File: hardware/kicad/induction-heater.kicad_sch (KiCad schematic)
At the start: 20 parts, among them Q1 Q_NMOS_DGS, Q2 Q_NMOS_DGS

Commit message: next
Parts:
- D1: Spice_Model D -> (none); Spice_Netlist_Enabled Y -> (none); Spice_Primitive D -> (none)
- D5: Spice_Model (none) -> D_Zener; Spice_Netlist_Enabled (none) -> Y; Spice_Primitive (none) -> D
- Q1, Q2: Spice_Model (none) -> Q_NMOS_DGS; Spice_Netlist_Enabled (none) -> Y; Spice_Primitive (none) -> M
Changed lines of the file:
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@@
     (effects (font (size 1.27 1.27)) (justify left bottom))
+  )
+  (symbol (lib_id "Device:D_Zener") (at 22.86 27.94 270) (unit 1)
+    (in_bom yes) (on_board yes) (fields_autoplaced)
+    (property "Reference" "D1" (id 0) (at 25.4 26.6699 90)
+      (effects (font (size 1.27 1.27)) (justify left))
+    )
+    (property "Value" "D_Zener" (id 1) (at 25.4 29.2099 90)
+      (effects (font (size 1.27 1.27)) (justify left))
+    )
+    (property "Footprint" "" (id 2) (at 22.86 27.94 0)
+      (effects (font (size 1.27 1.27)) hide)
+    )
+    (property "Datasheet" "~" (id 3) (at 22.86 27.94 0)
+      (effects (font (size 1.27 1.27)) hide)
+    )
+    (pin "1")
+    (pin "2")
   )
   (symbol (lib_id "power:GND") (at 111.76 88.9 0) (unit 1)
@@
       (effects (font (size 1.27 1.27)) hide)
     )
+    (property "Spice_Primitive" "M" (id 4) (at 134.62 76.2 0)
+      (effects (font (size 1.27 1.27)) hide)
+    )
+    (property "Spice_Model" "Q_NMOS_DGS" (id 5) (at 134.62 76.2 0)
+      (effects (font (size 1.27 1.27)) hide)
+    )
+    (property "Spice_Netlist_Enabled" "Y" (id 6) (at 134.62 76.2 0)
+      (effects (font (size 1.27 1.27)) hide)
+    )
     (pin "1")
     (pin "2")
@@
     )
     (property "Spice_Netlist_Enabled" "Y" (id 6) (at 111.76 68.58 0)
-      (effects (font (size 1.27 1.27)) hide)
-    )
-    (pin "1")
-    (pin "2")
-  )
-  (symbol (lib_id "Device:D_Zener") (at 22.86 27.94 270) (unit 1)
-    (in_bom yes) (on_board yes) (fields_autoplaced)
-    (property "Reference" "D1" (id 0) (at 25.4 26.6699 90)
-      (effects (font (size 1.27 1.27)) (justify left))
-    )
-    (property "Value" "D_Zener" (id 1) (at 25.4 29.2099 90)
-      (effects (font (size 1.27 1.27)) (justify left))
-    )
-    (property "Footprint" "" (id 2) (at 22.86 27.94 0)
-      (effects (font (size 1.27 1.27)) hide)
-    )
-    (property "Datasheet" "~" (id 3) (at 22.86 27.94 0)
-      (effects (font (size 1.27 1.27)) hide)
-    )
-    (property "Spice_Primitive" "D" (id 4) (at 22.86 27.94 0)
-      (effects (font (size 1.27 1.27)) hide)
-    )
-    (property "Spice_Model" "D" (id 5) (at 22.86 27.94 0)
-      (effects (font (size 1.27 1.27)) hide)
-    )
-    (property "Spice_Netlist_Enabled" "Y" (id 6) (at 22.86 27.94 0)
       (effects (font (size 1.27 1.27)) hide)
     )
@@
       (effects (font (size 1.27 1.27)) hide)
     )
+    (property "Spice_Primitive" "D" (id 4) (at 111.76 82.55 0)
+      (effects (font (size 1.27 1.27)) hide)
+    )
+    (property "Spice_Model" "D_Zener" (id 5) (at 111.76 82.55 0)
+      (effects (font (size 1.27 1.27)) hide)
+    )
+    (property "Spice_Netlist_Enabled" "Y" (id 6) (at 111.76 82.55 0)
+      (effects (font (size 1.27 1.27)) hide)
+    )
     (pin "1")
     (pin "2")
@@
     )
     (property "Datasheet" "~" (id 3) (at 134.62 38.1 0)
+      (effects (font (size 1.27 1.27)) hide)
+    )
+    (property "Spice_Primitive" "M" (id 4) (at 134.62 38.1 0)
+      (effects (font (size 1.27 1.27)) hide)
+    )
+    (property "Spice_Model" "Q_NMOS_DGS" (id 5) (at 134.62 38.1 0)
+      (effects (font (size 1.27 1.27)) hide)
+    )
+    (property "Spice_Netlist_Enabled" "Y" (id 6) (at 134.62 38.1 0)
       (effects (font (size 1.27 1.27)) hide)
     )
@@
       (reference "C3") (unit 1) (value "4.7u") (footprint "")
     )
-    (path "/2d14997f-3535-4ad5-9243-33af41ad51f4"
+    (path "/00a8d501-612a-44b1-8671-7a3ee3d8d8a2"
       (reference "D1") (unit 1) (value "D_Zener") (footprint "")
     )

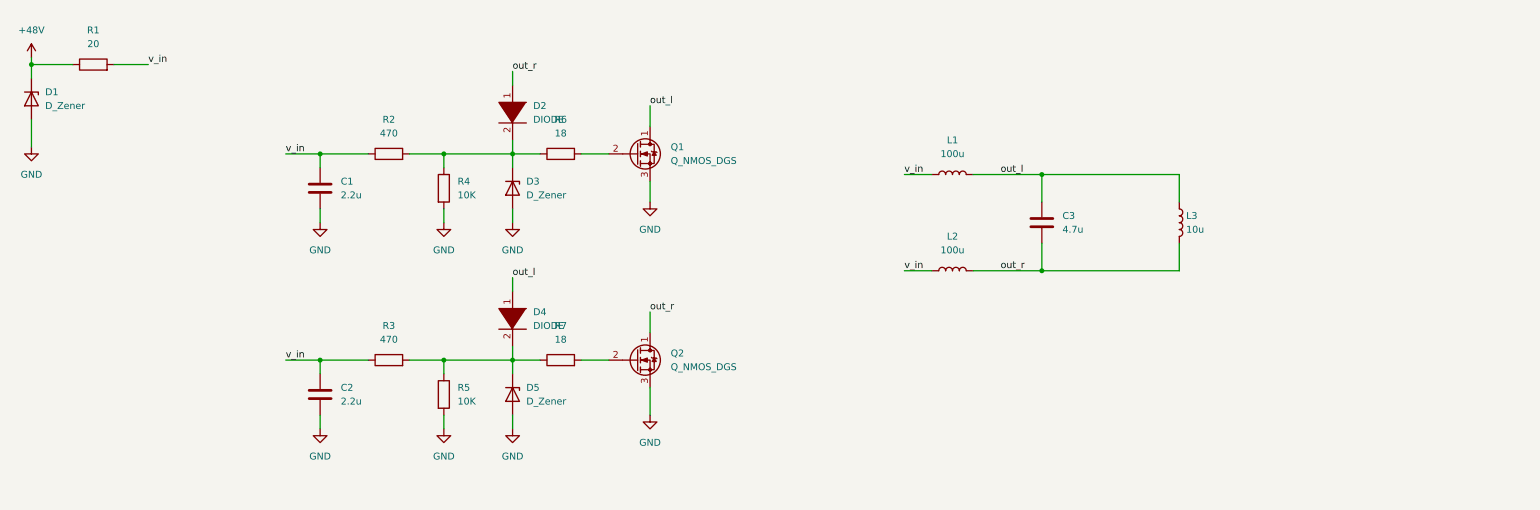
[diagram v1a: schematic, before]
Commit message: Components chosen and board layout made
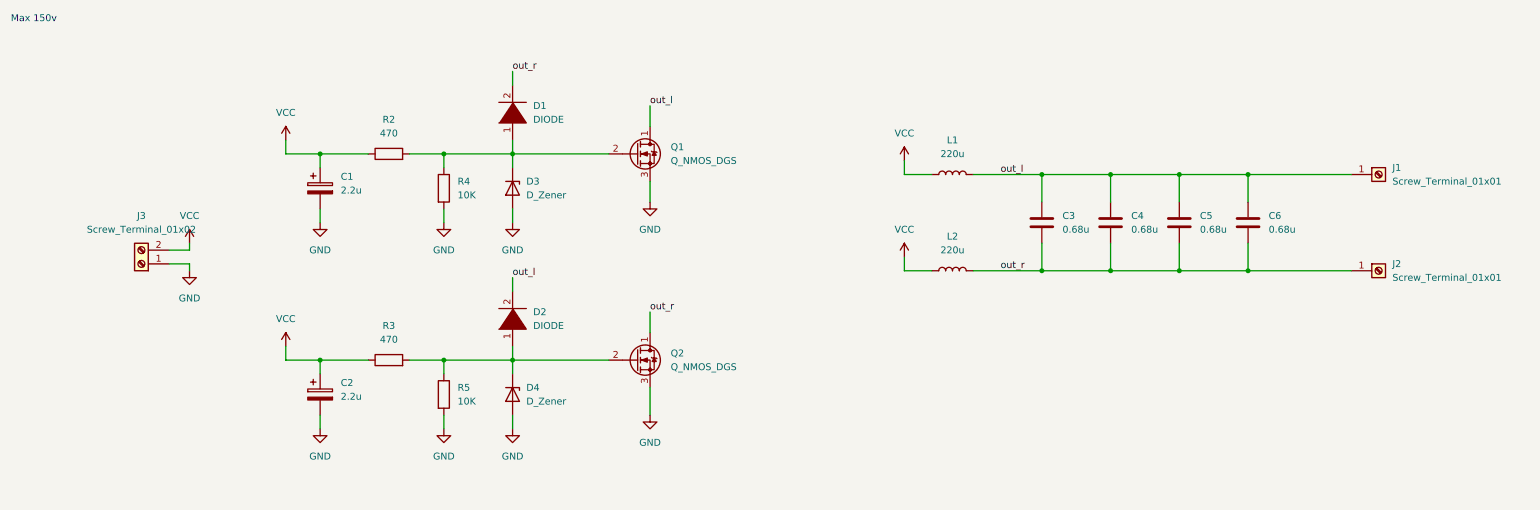
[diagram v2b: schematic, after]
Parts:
- removed C1, C2: 2.2u, symbol Device:C
- removed D1, D5: D_Zener, symbol Device:D_Zener
- removed D4: DIODE, symbol pspice:DIODE
- removed L3: 10u, symbol Device:L
- removed R1: 20, symbol Device:R
- removed R6, R7: 18, symbol Device:R
- added C1, C2: 2.2u, Capacitor_THT:CP_Radial_D6.3mm_P2.50mm, symbol Device:C_Polarized
- added C4, C5, C6: 0.68u, Capacitor_THT:C_Rect_L31.5mm_W15.0mm_P27.50mm_MKS4, symbol Device:C
- added D1: DIODE, Diode_THT:D_DO-41_SOD81_P7.62mm_Horizontal, symbol pspice:DIODE
- added D4: D_Zener, Diode_THT:D_DO-15_P12.70mm_Horizontal, symbol Device:D_Zener
- added J1, J2: Screw_Terminal_01x01, Connector:Banana_Jack_1Pin, symbol Connector:Screw_Terminal_01x01
- added J3: Screw_Terminal_01x02, Connector_Phoenix_MSTB:PhoenixContact_MSTBVA_2,5_2-G_1x02_P5.00mm_Vertical, symbol Connector:Screw_Terminal_01x02
- C3: value 4.7u -> 0.68u; footprint (none) -> Capacitor_THT:C_Rect_L31.5mm_W15.0mm_P27.50mm_MKS4; Max V (none) -> 1000; Mfr (none) -> MKS4O136806F00KYSD
- D2: footprint (none) -> Diode_THT:D_DO-41_SOD81_P7.62mm_Horizontal; Max V (none) -> 600; Mfr (none) -> UF4005-E3/54; Spice_Model DIODE -> (none); Spice_Netlist_Enabled Y -> (none); Spice_Primitive D -> (none)
- D3: footprint (none) -> Diode_THT:D_DO-15_P12.70mm_Horizontal; Mfr (none) -> 1N5349BG
- L1, L2: value 100u -> 220u; footprint (none) -> Inductor_THT:L_Toroid_Vertical_L31.8mm_W15.9mm_P13.50mm_Bourns_5700; Mfr (none) -> 2300HT-221-V-RC
- Q1, Q2: footprint (none) -> Package_TO_SOT_THT:TO-220-3_Vertical; Max V (none) -> 650; Mfr (none) -> NTP067N65S3H; Spice_Model Q_NMOS_DGS -> (none); Spice_Netlist_Enabled Y -> (none); Spice_Primitive M -> (none)
- R2, R3: footprint (none) -> Resistor_THT:R_Box_L8.4mm_W2.5mm_P5.08mm; Max V (none) -> 420; Mfr (none) -> AP851470RJ
- R4, R5: footprint (none) -> Resistor_THT:R_Axial_DIN0617_L17.0mm_D6.0mm_P20.32mm_Horizontal; Max V (none) -> 350; Mfr (none) -> ROX3SJ10K
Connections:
- net GND: now also C1.2, C2.2, D4.2 (A), J3.1 (Pin_1)
- net out_l: now also D2.2 (A), C4.1, C5.1, C6.1, J1.1 (Pin_1)
- net out_r: now also C4.2, C5.2, C6.2, D1.2 (A), J2.1 (Pin_1); no longer D2.1 (K)
- net at Q2.2 (G): now also D2.1 (K), R3.2, R5.1, D4.1 (K)
- net at D3.1 (K), R2.2, R4.1: now also Q1.2 (G), D1.1 (K); no longer D2.2 (A)
- net v_in renamed VCC
- net VCC: now also C1.1, C2.1, J3.2 (Pin_2)
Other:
- note added: "Max 150v"

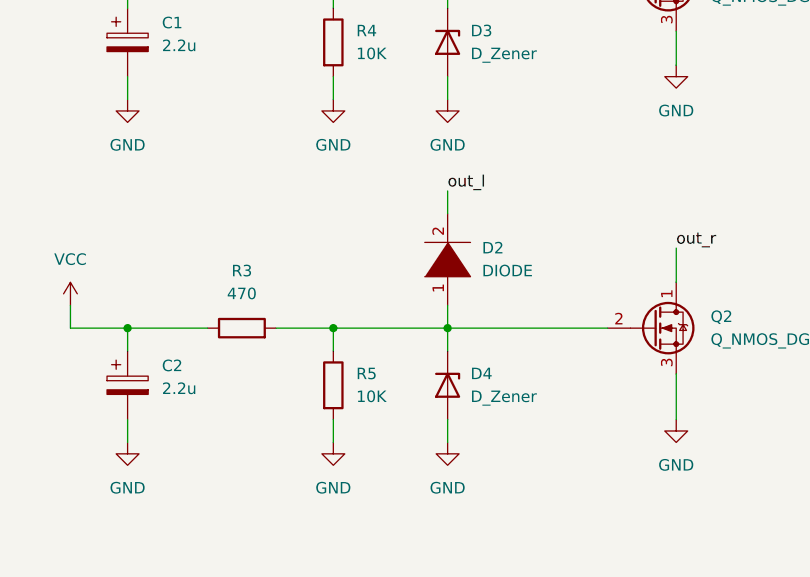
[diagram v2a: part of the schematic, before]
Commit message: Compacter board
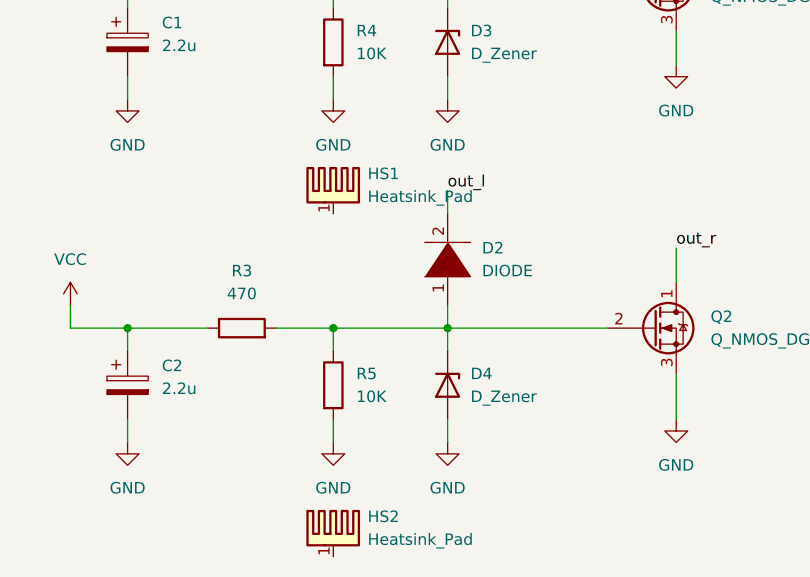
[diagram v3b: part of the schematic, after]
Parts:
- added HS1, HS2: Heatsink_Pad, Heatsink:Heatsink_Fischer_SK129-STS_42x25mm_2xDrill2.5mm, symbol Mechanical:Heatsink_Pad
- R4, R5: footprint Resistor_THT:R_Axial_DIN0617_L17.0mm_D6.0mm_P20.32mm_Horizontal -> Resistor_THT:R_Axial_DIN0207_L6.3mm_D2.5mm_P10.16mm_Horizontal
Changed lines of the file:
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@@
       (effects (font (size 1.27 1.27)) (justify left))
     )
-    (property "Footprint" "Resistor_THT:R_Axial_DIN0617_L17.0mm_D6.0mm_P20.32mm_Horizontal" (id 2) (at 97.282 82.55 90)
+    (property "Footprint" "Resistor_THT:R_Axial_DIN0207_L6.3mm_D2.5mm_P10.16mm_Horizontal" (id 2) (at 97.282 82.55 90)
       (effects (font (size 1.27 1.27)) hide)
     )
@@
     (pin "1")
     (pin "2")
+  )
+  (symbol (lib_id "Mechanical:Heatsink_Pad") (at 99.06 60.96 0) (unit 1)
+    (in_bom yes) (on_board yes) (fields_autoplaced)
+    (property "Reference" "HS1" (id 0) (at 102.87 59.0549 0)
+      (effects (font (size 1.27 1.27)) (justify left))
+    )
+    (property "Value" "Heatsink_Pad" (id 1) (at 102.87 61.5949 0)
+      (effects (font (size 1.27 1.27)) (justify left))
+    )
+    (property "Footprint" "Heatsink:Heatsink_Fischer_SK129-STS_42x25mm_2xDrill2.5mm" (id 2) (at 99.3648 62.23 0)
+      (effects (font (size 1.27 1.27)) hide)
+    )
+    (property "Datasheet" "~" (id 3) (at 99.3648 62.23 0)
+      (effects (font (size 1.27 1.27)) hide)
+    )
+    (property "Mfr" "6398BG" (id 4) (at 99.06 60.96 0)
+      (effects (font (size 1.27 1.27)) hide)
+    )
+    (pin "1")
   )
   (symbol (lib_id "power:VCC") (at 69.85 73.66 0) (unit 1)
@@
     (pin "1")
   )
+  (symbol (lib_id "Mechanical:Heatsink_Pad") (at 99.06 99.06 0) (unit 1)
+    (in_bom yes) (on_board yes) (fields_autoplaced)
+    (property "Reference" "HS2" (id 0) (at 102.87 97.1549 0)
+      (effects (font (size 1.27 1.27)) (justify left))
+    )
+    (property "Value" "Heatsink_Pad" (id 1) (at 102.87 99.6949 0)
+      (effects (font (size 1.27 1.27)) (justify left))
+    )
+    (property "Footprint" "Heatsink:Heatsink_Fischer_SK129-STS_42x25mm_2xDrill2.5mm" (id 2) (at 99.3648 100.33 0)
+      (effects (font (size 1.27 1.27)) hide)
+    )
+    (property "Datasheet" "~" (id 3) (at 99.3648 100.33 0)
+      (effects (font (size 1.27 1.27)) hide)
+    )
+    (property "Mfr" "6398BG" (id 4) (at 99.06 99.06 0)
+      (effects (font (size 1.27 1.27)) hide)
+    )
+    (pin "1")
+  )
   (symbol (lib_id "Device:R") (at 88.9 38.1 90) (unit 1)
     (in_bom yes) (on_board yes) (fields_autoplaced)
@@
       (effects (font (size 1.27 1.27)) (justify left))
     )
-    (property "Footprint" "Resistor_THT:R_Axial_DIN0617_L17.0mm_D6.0mm_P20.32mm_Horizontal" (id 2) (at 97.282 44.45 90)
+    (property "Footprint" "Resistor_THT:R_Axial_DIN0207_L6.3mm_D2.5mm_P10.16mm_Horizontal" (id 2) (at 97.282 44.45 90)
       (effects (font (size 1.27 1.27)) hide)
     )
@@
       (reference "D4") (unit 1) (value "D_Zener") (footprint "Diode_THT:D_DO-15_P12.70mm_Horizontal")
     )
+    (path "/834cb9dc-ce85-42d5-a7ea-3d0007b324dd"
+      (reference "HS1") (unit 1) (value "Heatsink_Pad") (footprint "Heatsink:Heatsink_Fischer_SK129-STS_42x25mm_2xDrill2.5mm")
+    )
+    (path "/e0b8b614-48b6-472f-8fc2-50e5877bdcf0"
+      (reference "HS2") (unit 1) (value "Heatsink_Pad") (footprint "Heatsink:Heatsink_Fischer_SK129-STS_42x25mm_2xDrill2.5mm")
+    )
     (path "/2eacdabb-611b-4761-b0ae-308768f69ecc"
       (reference "J1") (unit 1) (value "Screw_Terminal_01x01") (footprint "Connector:Banana_Jack_1Pin")
@@
     )
     (path "/f74691b4-ab73-45d2-adb2-a73aca070029"
-      (reference "R4") (unit 1) (value "10K") (footprint "Resistor_THT:R_Axial_DIN0617_L17.0mm_D6.0mm_P20.32mm_Horizontal")
+      (reference "R4") (unit 1) (value "10K") (footprint "Resistor_THT:R_Axial_DIN0207_L6.3mm_D2.5mm_P10.16mm_Horizontal")
     )
     (path "/799c8382-e657-4e5c-be05-62a7733f4321"
-      (reference "R5") (unit 1) (value "10K") (footprint "Resistor_THT:R_Axial_DIN0617_L17.0mm_D6.0mm_P20.32mm_Horizontal")
-    )
-  )
+      (reference "R5") (unit 1) (value "10K") (footprint "Resistor_THT:R_Axial_DIN0207_L6.3mm_D2.5mm_P10.16mm_Horizontal")
+    )
+  )

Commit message: Changed mfr to mpn
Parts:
- C1: MPN (none) -> ESL225M250AE3AA; Mfr ESL225M250AE3AA -> (none)
- C2: MPN (none) -> ESL225M250AE3AA; Mouser No 80-ESL225M250AE3AA -> (none)
- C3, C4, C5, C6: MPN (none) -> MKS4O136806F00KYSD; Mfr MKS4O136806F00KYSD -> (none)
- D1, D2: MPN (none) -> UF4005-E3/54; Mfr UF4005-E3/54 -> (none)
- D3, D4: MPN (none) -> 1N5927BRLG; Mfr 1N5349BG -> (none)
- HS1, HS2: MPN (none) -> 6398BG; Mfr 6398BG -> (none)
- J3: MPN (none) -> TB007-508-02BE; Mfr TB007-508-02BE -> (none)
- L1, L2: MPN (none) -> 2300HT-221-V-RC; Mfr 2300HT-221-V-RC -> (none)
- Q1, Q2: MPN (none) -> NTP067N65S3H; Mfr NTP067N65S3H -> (none)
- R2, R3: MPN (none) -> AP851470RJ; Mfr AP851470RJ -> (none)
- R4, R5: MPN (none) -> ROX3SJ10K; Mfr ROX3SJ10K -> (none)
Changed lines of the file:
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@@
       (effects (font (size 1.27 1.27)) hide)
     )
-    (property "Mfr" "NTP067N65S3H " (id 4) (at 134.62 76.2 0)
+    (property "MPN" "NTP067N65S3H " (id 4) (at 134.62 76.2 0)
       (effects (font (size 1.27 1.27)) hide)
     )
@@
       (effects (font (size 1.27 1.27)) hide)
     )
-    (property "Mfr" "AP851470RJ" (id 4) (at 88.9 76.2 90)
+    (property "MPN" "AP851470RJ" (id 4) (at 88.9 76.2 90)
       (effects (font (size 1.27 1.27)) hide)
     )
@@
       (effects (font (size 1.27 1.27)) hide)
     )
-    (property "Mfr" "UF4005-E3/54 " (id 4) (at 111.76 30.48 90)
+    (property "MPN" "UF4005-E3/54 " (id 4) (at 111.76 30.48 90)
       (effects (font (size 1.27 1.27)) hide)
     )
@@
       (effects (font (size 1.27 1.27)) hide)
     )
-    (property "Mfr" "MKS4O136806F00KYSD " (id 4) (at 247.65 50.8 0)
+    (property "MPN" "MKS4O136806F00KYSD " (id 4) (at 247.65 50.8 0)
       (effects (font (size 1.27 1.27)) hide)
     )
@@
       (effects (font (size 1.27 1.27)) hide)
     )
-    (property "Datasheet" "https://nl.mouser.com/datasheet/2/308/1N5333B_D-1801430.pdf" (id 3) (at 111.76 82.55 0)
-      (effects (font (size 1.27 1.27)) hide)
-    )
-    (property "Mfr" "1N5349BG " (id 4) (at 111.76 82.55 90)
+    (property "Datasheet" "https://nl.mouser.com/datasheet/2/308/1N5913B_D-1801544.pdf" (id 3) (at 111.76 82.55 0)
+      (effects (font (size 1.27 1.27)) hide)
+    )
+    (property "MPN" "1N5927BRLG" (id 4) (at 111.76 82.55 90)
       (effects (font (size 1.27 1.27)) hide)
     )
@@
       (effects (font (size 1.27 1.27)) hide)
     )
-    (property "Datasheet" "https://nl.mouser.com/datasheet/2/308/1N5333B_D-1801430.pdf" (id 3) (at 111.76 44.45 0)
-      (effects (font (size 1.27 1.27)) hide)
-    )
-    (property "Mfr" "1N5349BG " (id 4) (at 111.76 44.45 90)
+    (property "Datasheet" "https://nl.mouser.com/datasheet/2/308/1N5913B_D-1801544.pdf" (id 3) (at 111.76 44.45 0)
+      (effects (font (size 1.27 1.27)) hide)
+    )
+    (property "MPN" "1N5927BRLG" (id 4) (at 111.76 44.45 90)
       (effects (font (size 1.27 1.27)) hide)
     )
@@
       (effects (font (size 1.27 1.27)) hide)
     )
-    (property "Mfr" "ESL225M250AE3AA " (id 4) (at 76.2 44.45 0)
+    (property "MPN" "ESL225M250AE3AA " (id 4) (at 76.2 44.45 0)
       (effects (font (size 1.27 1.27)) hide)
     )
@@
       (effects (font (size 1.27 1.27)) hide)
     )
-    (property "Mfr" "2300HT-221-V-RC " (id 4) (at 193.04 59.69 90)
+    (property "MPN" "2300HT-221-V-RC " (id 4) (at 193.04 59.69 90)
       (effects (font (size 1.27 1.27)) hide)
     )
@@
       (effects (font (size 1.27 1.27)) hide)
     )
-    (property "Mouser No" "80-ESL225M250AE3AA " (id 4) (at 76.2 82.55 0)
+    (property "MPN" "ESL225M250AE3AA " (id 4) (at 76.2 82.55 0)
       (effects (font (size 1.27 1.27)) hide)
     )
@@
       (effects (font (size 1.27 1.27)) hide)
     )
-    (property "Mfr" "TB007-508-02BE " (id 4) (at 43.18 58.42 0)
+    (property "MPN" "TB007-508-02BE " (id 4) (at 43.18 58.42 0)
       (effects (font (size 1.27 1.27)) hide)
     )
@@
       (effects (font (size 1.27 1.27)) hide)
     )
-    (property "Mfr" "NTP067N65S3H " (id 4) (at 134.62 38.1 0)
+    (property "MPN" "NTP067N65S3H " (id 4) (at 134.62 38.1 0)
       (effects (font (size 1.27 1.27)) hide)
     )
@@
       (effects (font (size 1.27 1.27)) hide)
     )
-    (property "Mfr" "ROX3SJ10K" (id 4) (at 99.06 82.55 0)
+    (property "MPN" "ROX3SJ10K" (id 4) (at 99.06 82.55 0)
       (effects (font (size 1.27 1.27)) hide)
     )
@@
       (effects (font (size 1.27 1.27)) hide)
     )
-    (property "Mfr" "MKS4O136806F00KYSD " (id 4) (at 234.95 50.8 0)
+    (property "MPN" "MKS4O136806F00KYSD " (id 4) (at 234.95 50.8 0)
       (effects (font (size 1.27 1.27)) hide)
     )
@@
       (effects (font (size 1.27 1.27)) hide)
     )
-    (property "Mfr" "6398BG" (id 4) (at 99.06 60.96 0)
+    (property "MPN" "6398BG" (id 4) (at 99.06 60.96 0)
       (effects (font (size 1.27 1.27)) hide)
     )
@@
       (effects (font (size 1.27 1.27)) hide)
     )
-    (property "Mfr" "UF4005-E3/54 " (id 4) (at 111.76 68.58 90)
+    (property "MPN" "UF4005-E3/54 " (id 4) (at 111.76 68.58 90)
       (effects (font (size 1.27 1.27)) hide)
     )
@@
       (effects (font (size 1.27 1.27)) hide)
     )
-    (property "Mfr" "2300HT-221-V-RC " (id 4) (at 193.04 41.91 90)
+    (property "MPN" "2300HT-221-V-RC " (id 4) (at 193.04 41.91 90)
       (effects (font (size 1.27 1.27)) hide)
     )
@@
       (effects (font (size 1.27 1.27)) hide)
     )
-    (property "Mfr" "MKS4O136806F00KYSD " (id 4) (at 222.25 50.8 0)
+    (property "MPN" "MKS4O136806F00KYSD " (id 4) (at 222.25 50.8 0)
       (effects (font (size 1.27 1.27)) hide)
     )
@@
       (effects (font (size 1.27 1.27)) hide)
     )
-    (property "Mfr" "6398BG" (id 4) (at 99.06 99.06 0)
+    (property "MPN" "6398BG" (id 4) (at 99.06 99.06 0)
       (effects (font (size 1.27 1.27)) hide)
     )
@@
       (effects (font (size 1.27 1.27)) hide)
     )
-    (property "Mfr" "AP851470RJ" (id 4) (at 88.9 38.1 90)
+    (property "MPN" "AP851470RJ" (id 4) (at 88.9 38.1 90)
       (effects (font (size 1.27 1.27)) hide)
     )
@@
       (effects (font (size 1.27 1.27)) hide)
     )
-    (property "Mfr" "MKS4O136806F00KYSD " (id 4) (at 209.55 50.8 0)
+    (property "MPN" "MKS4O136806F00KYSD " (id 4) (at 209.55 50.8 0)
       (effects (font (size 1.27 1.27)) hide)
     )
@@
       (effects (font (size 1.27 1.27)) hide)
     )
-    (property "Mfr" "ROX3SJ10K" (id 4) (at 99.06 44.45 0)
-      (effects (font (size 1.27 1.27)) hide)
-    )
+    (property "MPN" "ROX3SJ10K" (id 4) (at 99.06 44.45 0)
+      (effects (font (size 1.27 1.27)) hide)
+    )
